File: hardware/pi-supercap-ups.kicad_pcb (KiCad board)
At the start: 2 copper layers, 65 x 56 mm, 69 parts, among them J1 Screw_Terminal_01x04, J2 Raspberry_Pi_2_3, U1 ATtiny13A-SSU, U2 MP1584EN, U3 MT3608, U4 MCP2515-xSO, U5 TJA1051T-3, U6 DS3231M, Y1 8MHz

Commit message: Implement next hardware revision
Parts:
- removed TP3: Vcap, TestPoint:TestPoint_Keystone_5000-5004_Miniature
- added C15: 150pF, Capacitor_SMD:C_0603_1608Metric_Pad1.05x0.95mm_HandSolder, F.Cu at (65.9, 69.1)
- added C16: 47uF, Capacitor_SMD:C_0805_2012Metric_Pad1.15x1.40mm_HandSolder, F.Cu at (65.8, 63.3)
- added C17: 47uF, Capacitor_SMD:C_0805_2012Metric_Pad1.15x1.40mm_HandSolder, F.Cu at (59.2, 55.4)
- added J3: Conn_01x08_Male, Connector_PinHeader_2.54mm:PinHeader_1x08_P2.54mm_Vertical, F.Cu at (66.0, 27.9)
- added J4: Conn_01x02_Male, Connector_PinHeader_2.54mm:PinHeader_1x02_P2.54mm_Vertical, F.Cu at (69.3, 50.0)
- added JP2: SolderJumper_2_Open, custom:SolderJumper-2_P1.3mm_OpenMask_RoundedPad1.0x1.5mm, F.Cu at (69.5, 27.9)
- added JP3: SolderJumper_2_Open, custom:SolderJumper-2_P1.3mm_OpenMask_RoundedPad1.0x1.5mm, F.Cu at (69.5, 43.2)
- added JP4: SolderJumper_2_Open, custom:SolderJumper-2_P1.3mm_OpenMask_RoundedPad1.0x1.5mm, F.Cu at (69.5, 40.6)
- added JP5: SolderJumper_2_Open, custom:SolderJumper-2_P1.3mm_OpenMask_RoundedPad1.0x1.5mm, F.Cu at (69.5, 38.1)
- added JP6: SolderJumper_2_Open, custom:SolderJumper-2_P1.3mm_OpenMask_RoundedPad1.0x1.5mm, F.Cu at (69.5, 33.0)
- added JP7: SolderJumper_3_Open, custom:SolderJumper-3_P1.3mm_OpenMask_RoundedPad1.0x1.5mm, F.Cu at (70.1, 30.5)
- added R17: 15k, Resistor_SMD:R_0603_1608Metric_Pad1.05x0.95mm_HandSolder, F.Cu at (55.5, 67.1)
- added R18: 6.8k, Resistor_SMD:R_0603_1608Metric_Pad1.05x0.95mm_HandSolder, F.Cu at (54.6, 71.3)
- added R19: 10k, Resistor_SMD:R_0603_1608Metric_Pad1.05x0.95mm_HandSolder, F.Cu at (61.5, 71.2)
- added R20: 2.2k, Resistor_SMD:R_0603_1608Metric_Pad1.05x0.95mm_HandSolder, F.Cu at (65.8, 54.2)
- added R21: 2.2k, Resistor_SMD:R_0603_1608Metric_Pad1.05x0.95mm_HandSolder, F.Cu at (65.8, 52.6)
- added TP8: Vbuck, TestPoint:TestPoint_Keystone_5000-5004_Miniature, F.Cu at (62.2, 67.3)
- added TP9: Vboost, TestPoint:TestPoint_Keystone_5000-5004_Miniature, F.Cu at (54.9, 54.2)
- added U7: MT9700, Package_TO_SOT_SMD:SOT-23-5_HandSoldering, F.Cu at (58.0, 71.1)
- C1: value 100nF -> 47uF; footprint Capacitor_SMD:C_0603_1608Metric_Pad1.05x0.95mm_HandSolder -> Capacitor_SMD:C_0805_2012Metric_Pad1.15x1.40mm_HandSolder
- C10: value 22pF -> 100nF
- C12: value 47uF -> 100nF; footprint Capacitor_SMD:C_0805_2012Metric_Pad1.15x1.40mm_HandSolder -> Capacitor_SMD:C_0603_1608Metric_Pad1.05x0.95mm_HandSolder
- C13: value 100nF -> 10uF; footprint Capacitor_SMD:C_0603_1608Metric_Pad1.05x0.95mm_HandSolder -> Capacitor_SMD:C_0805_2012Metric_Pad1.15x1.40mm_HandSolder
- C2: value 10F -> 100nF; footprint Capacitor_THT:CP_Radial_D10.0mm_P5.00mm -> Capacitor_SMD:C_0603_1608Metric_Pad1.05x0.95mm_HandSolder
- C4: value 10uF -> 10F; footprint Capacitor_SMD:C_0805_2012Metric_Pad1.15x1.40mm_HandSolder -> Capacitor_THT:CP_Radial_D10.0mm_P5.00mm
- C5: value 100nF -> 10F; footprint Capacitor_SMD:C_0603_1608Metric_Pad1.05x0.95mm_HandSolder -> Capacitor_THT:CP_Radial_D10.0mm_P5.00mm
- C6: value 150pF -> 10F; footprint Capacitor_SMD:C_0603_1608Metric_Pad1.05x0.95mm_HandSolder -> Capacitor_THT:CP_Radial_D10.0mm_P5.00mm
- C7, C8: value 47uF -> 22pF; footprint Capacitor_SMD:C_0805_2012Metric_Pad1.15x1.40mm_HandSolder -> Capacitor_SMD:C_0603_1608Metric_Pad1.05x0.95mm_HandSolder
- C9: value 22pF -> 47uF; footprint Capacitor_SMD:C_0603_1608Metric_Pad1.05x0.95mm_HandSolder -> Capacitor_SMD:C_0805_2012Metric_Pad1.15x1.40mm_HandSolder
- D1: value RLED -> SMF16CA; footprint LED_SMD:LED_0603_1608Metric_Pad1.05x0.95mm_HandSolder -> Diode_SMD:D_SOD-123F
- D10, D11: value DS34W -> GLED; footprint Diode_SMD:D_SOD-123F -> LED_SMD:LED_0603_1608Metric_Pad1.05x0.95mm_HandSolder
- D12: value RLED -> DS34W; footprint Diode_SMD:D_0603_1608Metric_Pad1.05x0.95mm_HandSolder -> Diode_SMD:D_SOD-123F
- D13, D14: value GLED -> DS34W; footprint LED_SMD:LED_0603_1608Metric_Pad1.05x0.95mm_HandSolder -> Diode_SMD:D_SOD-123F
- D2: value Zener 3V3 -> DS34W; footprint Diode_SMD:D_SOD-123 -> Diode_SMD:D_SOD-123F
- D3: value DS34W -> RLED; footprint Diode_SMD:D_SOD-123F -> Diode_SMD:D_0603_1608Metric_Pad1.05x0.95mm_HandSolder
- D4, D5: value ZMM55C2V7 -> RLED; footprint Diode_SMD:D_MiniMELF_Handsoldering -> Diode_SMD:D_0603_1608Metric_Pad1.05x0.95mm_HandSolder
- D6: value DS34W -> RLED; footprint Diode_SMD:D_SOD-123F -> LED_SMD:LED_0603_1608Metric_Pad1.05x0.95mm_HandSolder
- D7: value RLED -> Zener 3V3; footprint Diode_SMD:D_0603_1608Metric_Pad1.05x0.95mm_HandSolder -> Diode_SMD:D_SOD-123
- D8: value RLED -> ZMM55C2V7; footprint Diode_SMD:D_0603_1608Metric_Pad1.05x0.95mm_HandSolder -> Diode_SMD:D_MiniMELF_Handsoldering
- D9: value DS34W -> ZMM55C2V7; footprint Diode_SMD:D_SOD-123F -> Diode_SMD:D_MiniMELF_Handsoldering
- J1: footprint TerminalBlock_MetzConnect:TerminalBlock_MetzConnect_Type055_RT01504HDWU_1x04_P5.00mm_Horizontal -> custom:15EDGVC-3.81-4P
- L2: value 4.7uH -> 5.6uH
- R1: value 680R -> 4.7k
- R10: value 110k -> 2.2k
- R11: value 15k -> 120R; footprint Resistor_SMD:R_0603_1608Metric_Pad1.05x0.95mm_HandSolder -> Resistor_SMD:R_1206_3216Metric_Pad1.42x1.75mm_HandSolder
- R12: value 1k -> 100k
- R13: value 10k -> 100k
- R14: value 1k -> 40.2k
- R15: value 1k -> 210k
- R16: value 120R -> 110k; footprint Resistor_SMD:R_1206_3216Metric_Pad1.42x1.75mm_HandSolder -> Resistor_SMD:R_0603_1608Metric_Pad1.05x0.95mm_HandSolder
- R2: value 4.7k -> 2.2k
- R3: value 20R -> 2.2k; footprint Resistor_SMD:R_2512_6332Metric_Pad1.52x3.35mm_HandSolder -> Resistor_SMD:R_0603_1608Metric_Pad1.05x0.95mm_HandSolder
- R4: value 1k -> 1.5k
- R5: value 3k -> 4.7k
- R6: value 100k -> 4.7k
- R7: value 100k -> 10k
- R8: value 40.2k -> 10k
- R9: value 210k -> 2.2k
- TP1: value GND -> +12V_prot
- TP2: value Sense_Vcc -> GND
- TP4: value Vout -> Vcap
- U2: value MP1584EN -> MCP2515-xSO; footprint Package_SO:SOIC-8-1EP_3.9x4.9mm_P1.27mm_EP2.35x2.35mm -> Package_SO:SOIC-18W_7.5x11.6mm_P1.27mm
- U3: value MT3608 -> TJA1051T-3; footprint Package_TO_SOT_SMD:SOT-23-6_Handsoldering -> Package_SO:SOIC-8_3.9x4.9mm_P1.27mm
- U4: value MCP2515-xSO -> DS3231M; footprint Package_SO:SOIC-18W_7.5x11.6mm_P1.27mm -> Package_SO:SOIC-16W_7.5x10.3mm_P1.27mm
- U5: value TJA1051T-3 -> MP1584EN; footprint Package_SO:SOIC-8_3.9x4.9mm_P1.27mm -> Package_SO:SOIC-8-1EP_3.9x4.9mm_P1.27mm_EP2.35x2.35mm
- U6: value DS3231M -> MT3608; footprint Package_SO:SOIC-16W_7.5x10.3mm_P1.27mm -> Package_TO_SOT_SMD:SOT-23-6_Handsoldering
- moved C13 64.2 mm to (77.5, 67.3), turned to 0 degrees
- moved R2 56.0 mm to (23.4, 59.3)
- moved D1 52.7 mm to (80.3, 46.8), turned to 90 degrees
- moved R9 51.5 mm to (27.9, 43.8), turned to 90 degrees
- moved D10 49.6 mm to (26.2, 43.8), turned to 90 degrees
- moved R12 49.5 mm to (76.5, 70.5), turned to 270 degrees
- moved C1 48.8 mm to (24.9, 26.9)
- moved D7 47.9 mm to (75.3, 47.1), turned to 270 degrees
- moved D6 47.7 mm to (21.3, 29.9), turned to 90 degrees
- moved R8 46.0 mm to (52.1, 29.0), turned to 270 degrees
- moved D12 45.9 mm to (69.2, 64.3), turned to 180 degrees
- moved TP2 45.6 mm to (32.1, 44.7)
- moved R14 42.8 mm to (69.8, 72.1), turned to 0 degrees
- moved R7 42.7 mm to (54.9, 27.8), turned to 270 degrees
- moved U2 42.4 mm to (45.2, 33.7)
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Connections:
- C1 pad 1: 3.3V -> /5V
- C10 pad 1: /CANbus interface/OSC1 -> GND
- C10 pad 2: GND -> 3.3V
- C11 pad 1: 3.3V -> GND
- C11 pad 2: GND -> /5V
- C12 pad 1: GND -> 3.3V
- C12 pad 2: /5V -> GND
- C13 pad 1: 3.3V -> /inv_Sense_Vcc/+12V
- C14 pad 1: GND -> /Buck converter/SW
- C14 pad 2: 3.3V -> /Buck converter/BST
- C2 pad 1: /Power Bank/Vcap -> 3.3V
- C2 pad 2: /Power Bank/Vc1 -> GND
- C3 pad 1: /Power Bank/Vc1 -> /Power Bank/Vcap
- C3 pad 2: GND -> /Power Bank/Vc1
- C4 pad 1: /Voltage input/+12V_protected -> /Power Bank/Vc1
- C5 pad 1: /Voltage input/SW -> /Power Bank/Vcap
- C5 pad 2: /Voltage input/BST -> /Power Bank/Vc1
- C6 pad 1: /Voltage input/COMP -> /Power Bank/Vc1
- C6 pad 2: Net-(C6-Pad2) -> GND
- C7 pad 1: /Power Bank/Vin -> GND
- C7 pad 2: GND -> /CANbus interface/OSC2
- C8 pad 1: /5V -> /CANbus interface/OSC1
- C9 pad 1: GND -> 3.3V
- C9 pad 2: /CANbus interface/OSC2 -> GND
- D1 pad 1: GND -> /12V_fused
- D1 pad 2: Net-(D1-Pad2) -> GND
- D10 pad 1: /Voltage input/SW -> GND
- D10 pad 2: GND -> Net-(D10-Pad2)
- D11 pad 1: /5V -> GND
- D11 pad 2: /Voltage output/SW -> Net-(D11-Pad2)
- D12 pad 1: GND -> /Buck converter/SW
- D12 pad 2: Net-(D12-Pad2) -> GND
- D13 pad 1: GND -> /5V
- D13 pad 2: Net-(D13-Pad2) -> /Current limiting/Vin
- D14 pad 1: GND -> /5V
- D14 pad 2: Net-(D14-Pad2) -> /Boost converter/SW
- D2 pad 1: /Sense_Vcc -> /inv_Sense_Vcc/+12V
- D2 pad 2: GND -> /12V_fused
- D3 pad 1: /Power Bank/Vout -> GND
- D3 pad 2: /Power Bank/Vin -> Net-(D3-Pad2)
- D4 pad 1: /Power Bank/Vcap -> GND
- D4 pad 2: /Power Bank/Vc1 -> Net-(D4-Pad2)
- D5 pad 1: /Power Bank/Vc1 -> GND
- D5 pad 2: GND -> Net-(D5-Pad2)
- D6 pad 1: /Power Bank/Vout -> GND
- D6 pad 2: /Power Bank/Vcap -> Net-(D6-Pad2)
- D7 pad 1: GND -> /Sense_Vcc
- D7 pad 2: Net-(D7-Pad2) -> GND
- D8 pad 1: GND -> /Power Bank/Vcap
- D8 pad 2: Net-(D8-Pad2) -> /Power Bank/Vc1
- D9 pad 1: /Voltage input/+12V_protected -> /Power Bank/Vc1
- D9 pad 2: /Voltage input/12V_fused -> GND
- F1 pad 1: /Voltage input/12V_fused -> /12V_fused
- J2 pad 35: /MISO -> /GPIO19
- J2 pad 36: /ATTiny_RESET -> /GPIO16
- J2 pad 37: /Sense_Vcc -> /GPIO26
- J2 pad 38: /inv_Sense_EN -> /GPIO20
- J2 pad 40: /ATSCK -> /GPIO21
- L1 pad 1: /Voltage input/SW -> /Buck converter/SW
- L1 pad 2: /Power Bank/Vin -> /Current limiting/Vin
- L2 pad 1: /Power Bank/Vout -> /Power Bank/Vcap
- L2 pad 2: /Voltage output/SW -> /Boost converter/SW
- R1 pad 1: 3.3V -> /inv_Sense_Vcc/+12V
- R1 pad 2: Net-(D1-Pad2) -> Net-(D3-Pad2)
- R10 pad 1: /5V -> /CANbus interface/RX
- R10 pad 2: /Voltage output/FB -> Net-(D11-Pad2)
- R11 pad 1: /Voltage output/FB -> Net-(JP1-Pad2)
- R11 pad 2: GND -> /CAN_H
- R12 pad 1: /5V -> /Buck converter/FREQ
- R12 pad 2: Net-(D12-Pad2) -> GND
- R13 pad 1: 3.3V -> Net-(C15-Pad2)
- R13 pad 2: Net-(R13-Pad2) -> GND
- R14 pad 1: /CANbus interface/TX -> /Buck converter/FB
- R14 pad 2: Net-(D13-Pad2) -> GND
- R15 pad 1: /CANbus interface/RX -> /Buck converter/FB
- R15 pad 2: Net-(D14-Pad2) -> /5V
- R16 pad 1: Net-(JP1-Pad2) -> /Boost converter/SW
- R16 pad 2: /CAN_H -> /Boost converter/FB
- R2 pad 1: /Voltage input/+12V_protected -> /Power Bank/Vcap
- R2 pad 2: /Sense_Vcc -> Net-(D4-Pad2)
- R3 pad 1: /Power Bank/Vout -> /5V
- R3 pad 2: /Power Bank/Vcap -> Net-(D5-Pad2)
- R4 pad 1: /Power Bank/Vcap -> 3.3V
- R4 pad 2: Net-(D7-Pad2) -> Net-(D6-Pad2)
- R5 pad 1: /Voltage input/+12V_protected -> /Sense_Vcc
- R5 pad 2: Net-(D8-Pad2) -> GND
- R6 pad 1: /Voltage input/FREQ -> /inv_Sense_Vcc/+12V
- R6 pad 2: GND -> /Sense_Vcc
- R7 pad 1: Net-(C6-Pad2) -> 3.3V
- R7 pad 2: GND -> /ATTiny_RESET
- R8 pad 1: /Voltage input/FB -> 3.3V
- R8 pad 2: GND -> Net-(R8-Pad2)
- R9 pad 1: /Voltage input/FB -> /CANbus interface/TX
- R9 pad 2: /Power Bank/Vin -> Net-(D10-Pad2)
- TP1 pad 1: GND -> /inv_Sense_Vcc/+12V
- TP2 pad 1: /Sense_Vcc -> GND
- TP4 pad 1: /Power Bank/Vout -> /Power Bank/Vcap
- U1 pad 2: /Sense_Vcc -> /PB3
- U1 pad 3: /GPIO3 -> /PB4
- U1 pad 5: /inv_Sense_EN -> /MOSI
- U2 pad 1: /Voltage input/SW -> /CANbus interface/TX
- U2 pad 2: (no net) -> /CANbus interface/RX
- U2 pad 3: /Voltage input/COMP -> (no net)
- U2 pad 4: /Voltage input/FB -> (no net)
- U2 pad 5: GND -> (no net)
- U2 pad 6: /Voltage input/FREQ -> (no net)
- U2 pad 7: /Voltage input/+12V_protected -> /CANbus interface/OSC2
- U2 pad 8: /Voltage input/BST -> /CANbus interface/OSC1
- U2 pad 9: (no net) -> GND
- U3 pad 1: /Voltage output/SW -> /CANbus interface/TX
- U3 pad 3: /Voltage output/FB -> /5V
- U3 pad 4: /Power Bank/Vout -> /CANbus interface/RX
- U3 pad 5: /Power Bank/Vout -> 3.3V
- U3 pad 6: (no net) -> /CAN_L
- U4 pad 1: /CANbus interface/TX -> (no net)
- U4 pad 10: (no net) -> GND
- U4 pad 11: (no net) -> GND
- U4 pad 12: /INT -> GND
- U4 pad 13: /SCK -> GND
- U4 pad 14: /SI -> /RTC interface/VBAT
- U4 pad 15: /SO -> /SDA1
- U4 pad 16: /CS -> /GPIO3
- U4 pad 2: /CANbus interface/RX -> 3.3V
- U4 pad 5: (no net) -> GND
- U4 pad 6: (no net) -> GND
- U4 pad 7: /CANbus interface/OSC2 -> GND
- U4 pad 8: /CANbus interface/OSC1 -> GND
- U5 pad 1: /CANbus interface/TX -> /Buck converter/SW
- U5 pad 2: GND -> (no net)
- U5 pad 3: /5V -> /Buck converter/COMP
- U5 pad 4: /CANbus interface/RX -> /Buck converter/FB
- U5 pad 5: 3.3V -> GND
- U5 pad 6: /CAN_L -> /Buck converter/FREQ
- U5 pad 7: /CAN_H -> /inv_Sense_Vcc/+12V
- U5 pad 8: GND -> /Buck converter/BST
- U6 pad 1: (no net) -> /Boost converter/SW
- U6 pad 2: 3.3V -> GND
- U6 pad 3: (no net) -> /Boost converter/FB
- U6 pad 4: (no net) -> /Power Bank/Vcap
- U6 pad 5: GND -> /Power Bank/Vcap
- U6 pad 6: GND -> (no net)
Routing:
- net /inv_Sense_Vcc/+12V: track 0.00 -> 99.4 mm, vias 0 -> 6
- net /Voltage input/+12V_protected: track 80.5 -> 0.00 mm, vias 4 -> 0
- net /5V: track 116.2 -> 148.4 mm, vias 8 -> 9
- net /Power Bank/Vin: track 29.3 -> 0.00 mm, vias 2 -> 0
- net /GPIO21: track 0.00 -> 28.2 mm, vias 0 -> 1
- net 3.3V: track 113.4 -> 86.8 mm
- net /Power Bank/Vout: track 26.5 -> 0.00 mm
- net /Power Bank/Vc1: track 19.7 -> 41.7 mm, vias 0 -> 2
- net /CANbus interface/TX: track 73.1 -> 51.3 mm, vias 6 -> 4
- net /PB3: track 0.00 -> 21.1 mm, vias 0 -> 4
- net /GPIO20: track 0.00 -> 20.6 mm, vias 0 -> 1
- net /Power Bank/Vcap: track 52.4 -> 72.1 mm
- net /GPIO19: track 0.00 -> 19.6 mm, vias 0 -> 1
- net /Sense_Vcc: track 52.2 -> 33.8 mm, vias 4 -> 3
- net /Current limiting/Vin: track 0.00 -> 17.9 mm
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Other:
- outline, holes or cut-outs redrawn
- board text added: "+"
- board text added: "-"
- board text added: "H"
- board text added: "L"
- board text added: "Pi Super UPS revD Matti Airas 2019"
- board text removed: "12V"
- board text removed: "3.3V"
- board text removed: "5V"
- board text removed: "Pi Super UPS revC Matti Airas 2019"
- board text removed: "RX"
- board text removed: "TX"
- board text removed: "Vcap"

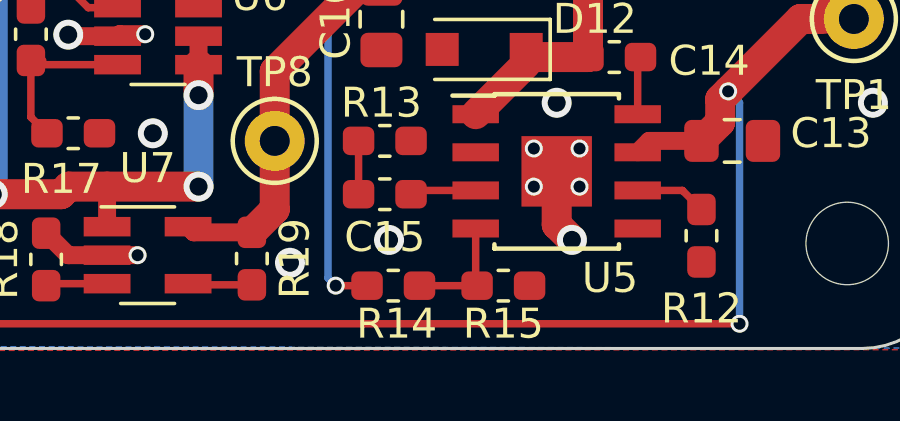
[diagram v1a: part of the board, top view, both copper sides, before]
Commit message: fix a silk screen error by swapping R14 and R15
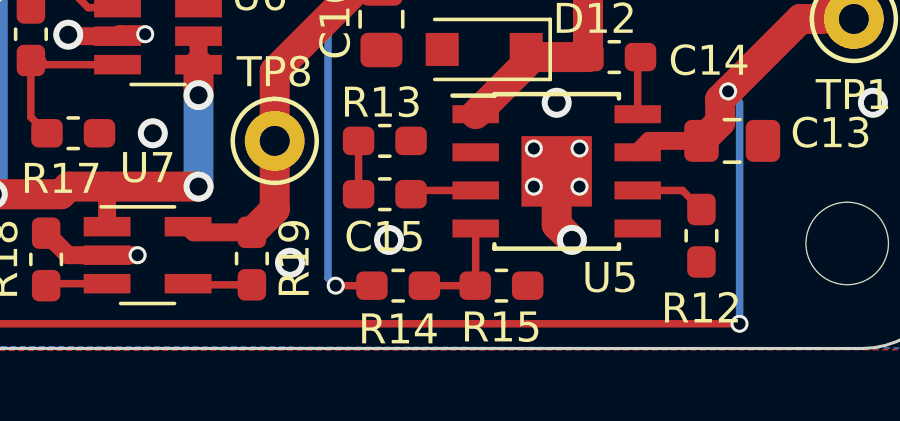
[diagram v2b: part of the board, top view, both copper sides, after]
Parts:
- R14: value 40.2k -> 210k
- R15: value 210k -> 40.2k
- moved R15 3.61 mm to (69.8, 72.1), turned to 0 degrees
- moved R14 3.51 mm to (66.3, 72.1), turned to 180 degrees
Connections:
- J2 pad 10: (no net) -> Net-(J2-Pad10)
- J2 pad 11: (no net) -> Net-(J2-Pad11)
- J2 pad 12: (no net) -> Net-(J2-Pad12)
- J2 pad 13: (no net) -> Net-(J2-Pad13)
- J2 pad 15: (no net) -> Net-(J2-Pad15)
- J2 pad 16: (no net) -> Net-(J2-Pad16)
- J2 pad 18: (no net) -> Net-(J2-Pad18)
- J2 pad 26: (no net) -> Net-(J2-Pad26)
- J2 pad 27: (no net) -> Net-(J2-Pad27)
- J2 pad 28: (no net) -> Net-(J2-Pad28)
- J2 pad 29: (no net) -> Net-(J2-Pad29)
- J2 pad 31: (no net) -> Net-(J2-Pad31)
- J2 pad 32: (no net) -> Net-(J2-Pad32)
- J2 pad 33: (no net) -> Net-(J2-Pad33)
- J2 pad 7: (no net) -> Net-(J2-Pad7)
- J2 pad 8: (no net) -> Net-(J2-Pad8)
- R14 pad 2: GND -> /5V
- R15 pad 2: /5V -> GND
- U2 pad 10: (no net) -> Net-(U2-Pad10)
- U2 pad 11: (no net) -> Net-(U2-Pad11)
- U2 pad 3: (no net) -> Net-(U2-Pad3)
- U2 pad 4: (no net) -> Net-(U2-Pad4)
- U2 pad 5: (no net) -> Net-(U2-Pad5)
- U2 pad 6: (no net) -> Net-(U2-Pad6)
- U4 pad 1: (no net) -> Net-(U4-Pad1)
- U4 pad 3: (no net) -> Net-(U4-Pad3)
- U4 pad 4: (no net) -> Net-(U4-Pad4)
- U5 pad 2: (no net) -> Net-(U5-Pad2)

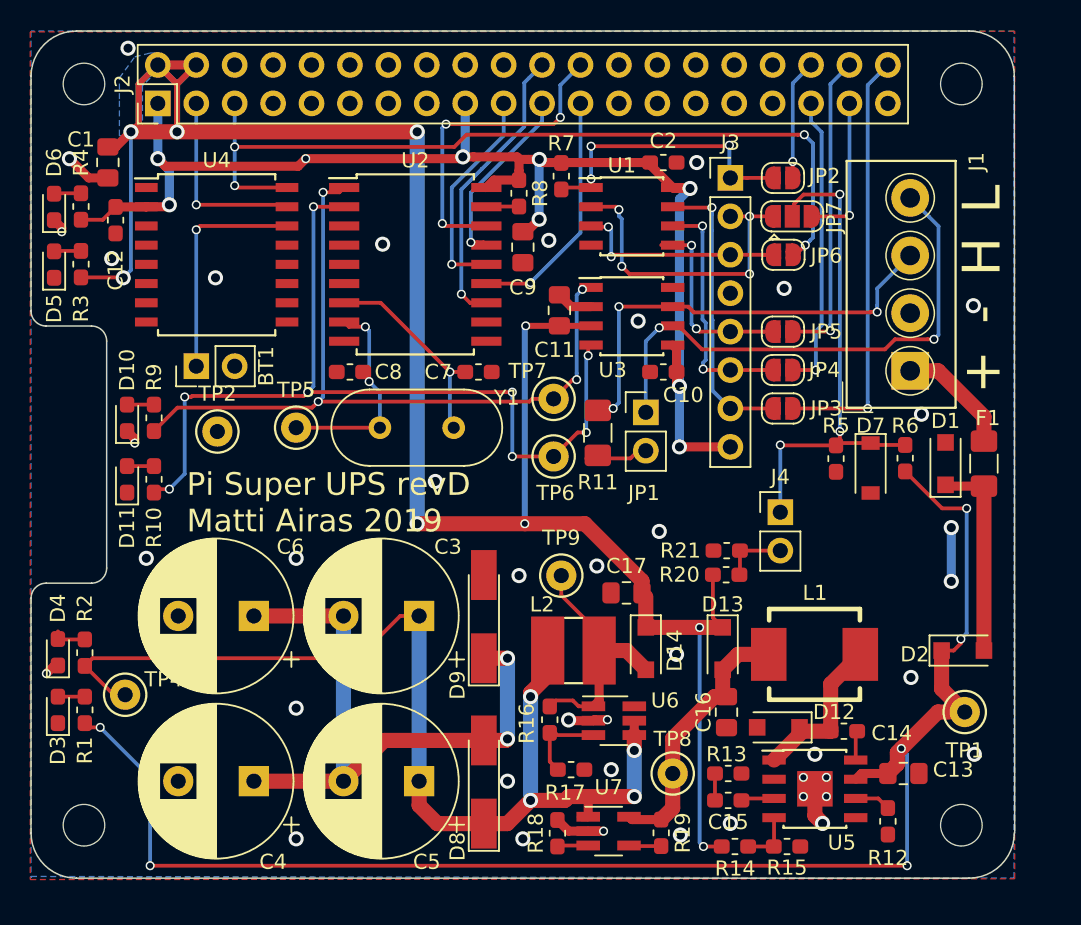
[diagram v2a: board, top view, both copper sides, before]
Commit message: Changed to pure-serial topology. Changed to beefier mcu.
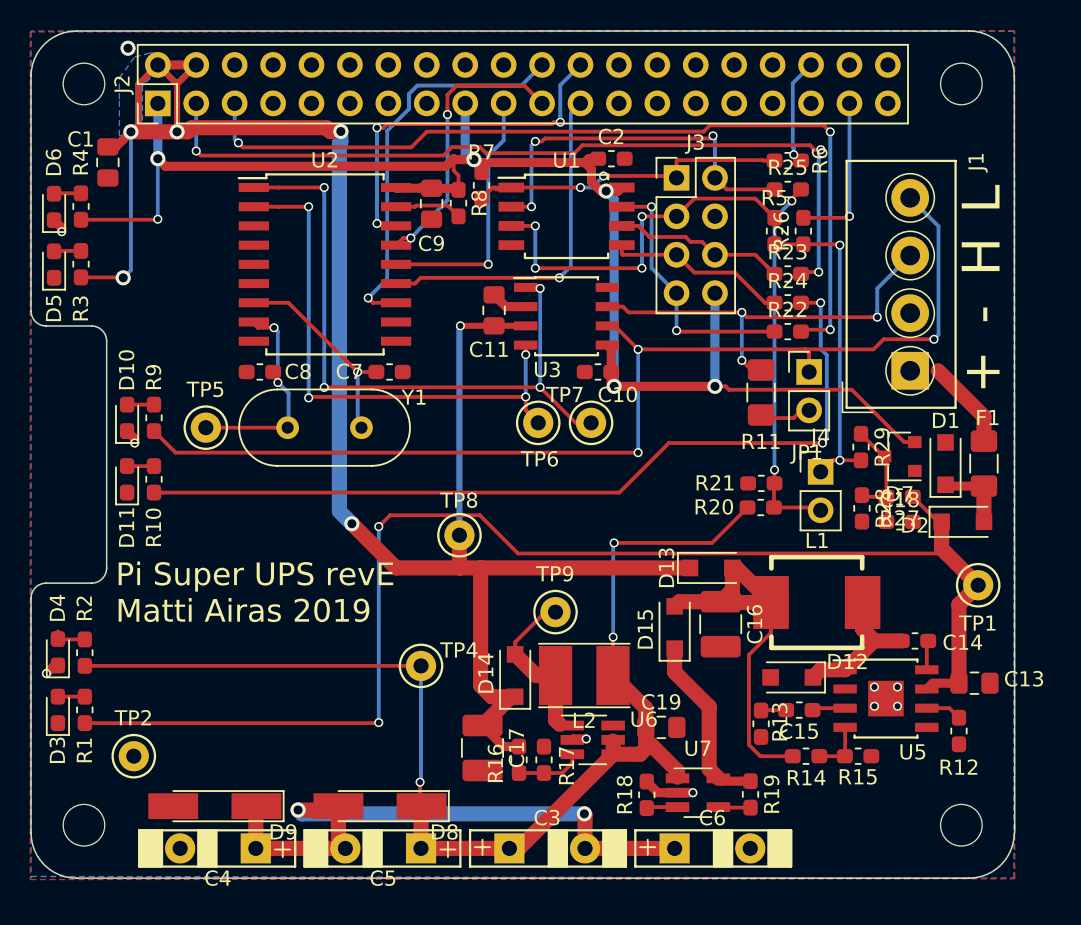
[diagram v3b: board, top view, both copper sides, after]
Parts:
- removed BT1: CR1220 3V, Connector_PinHeader_2.54mm:PinHeader_1x02_P2.54mm_Vertical
- removed C12: 100nF, Capacitor_SMD:C_0603_1608Metric_Pad1.05x0.95mm_HandSolder
- removed JP2, JP3, JP4, JP5, JP6: SolderJumper_2_Open, custom:SolderJumper-2_P1.3mm_OpenMask_RoundedPad1.0x1.5mm
- removed JP7: SolderJumper_3_Open, custom:SolderJumper-3_P1.3mm_OpenMask_RoundedPad1.0x1.5mm
- removed U4: DS3231M, Package_SO:SOIC-16W_7.5x10.3mm_P1.27mm
- added C18: 100nF, Capacitor_SMD:C_0603_1608Metric_Pad1.05x0.95mm_HandSolder, F.Cu at (77.2, 50.7)
- added C19: 22uF, Capacitor_SMD:C_0805_2012Metric_Pad1.15x1.40mm_HandSolder, F.Cu at (61.5, 64.3)
- added D15: DS34W, Diode_SMD:D_SOD-123F, F.Cu at (62.4, 57.7)
- added R22: 0, Resistor_SMD:R_0603_1608Metric_Pad1.05x0.95mm_HandSolder, F.Cu at (69.8, 38.1)
- added R23: 0, Resistor_SMD:R_0603_1608Metric_Pad1.05x0.95mm_HandSolder, F.Cu at (69.8, 34.3)
- added R24: 0, Resistor_SMD:R_0603_1608Metric_Pad1.05x0.95mm_HandSolder, F.Cu at (69.8, 36.2)
- added R25: 0, Resistor_SMD:R_0603_1608Metric_Pad1.05x0.95mm_HandSolder, F.Cu at (69.8, 28.7)
- added R26: 0, Resistor_SMD:R_0603_1608Metric_Pad1.05x0.95mm_HandSolder, F.Cu at (70.9, 31.5)
- added R27: 4.7k, Resistor_SMD:R_0603_1608Metric_Pad1.05x0.95mm_HandSolder, F.Cu at (77.2, 49.0)
- added R28: 10k, Resistor_SMD:R_0603_1608Metric_Pad1.05x0.95mm_HandSolder, F.Cu at (74.7, 49.8)
- added R29: 10k, Resistor_SMD:R_0603_1608Metric_Pad1.05x0.95mm_HandSolder, F.Cu at (74.7, 45.7)
- C16, C17: value 47uF -> 100uF; footprint Capacitor_SMD:C_0805_2012Metric_Pad1.15x1.40mm_HandSolder -> Capacitor_SMD:C_1210_3225Metric_Pad1.42x2.65mm_HandSolder
- C3, C4, C5, C6: footprint Capacitor_THT:CP_Radial_D10.0mm_P5.00mm -> custom:CP_Radial_D10.0mm_P5.00mm_flat
- D11: value GLED -> RLED
- D7: value Zener 3V3 -> BAT54S; footprint Diode_SMD:D_SOD-123 -> Package_TO_SOT_SMD:SOT-23
- J3: footprint Connector_PinHeader_2.54mm:PinHeader_1x08_P2.54mm_Vertical -> Connector_PinHeader_2.54mm:PinHeader_2x04_P2.54mm_Vertical
- L2: footprint Inductor_SMD:L_4.5x4.8_H3_Handsolder -> Inductor_SMD:L_Taiyo-Yuden_NR-40xx_HandSoldering
- R10: value 2.2k -> 1.5k
- R14: value 210k -> 232k
- R5, R6: value 4.7k -> 0
- U1: value ATtiny13A-SSU -> ATtiny25-20SU; footprint Package_SO:SOIC-8_3.9x4.9mm_P1.27mm -> Package_SO:SOIJ-8_5.3x5.3mm_P1.27mm
- moved C6 31.8 mm to (62.4, 72.3), turned to 0 degrees
- moved TP2 22.2 mm to (26.6, 66.2)
- moved D9 21.8 mm to (32.0, 69.5), turned to 180 degrees
- moved R6 21.1 mm to (69.8, 26.8), turned to 0 degrees
- moved TP8 21.1 mm to (48.1, 51.6)
- moved TP4 19.7 mm to (45.6, 60.2)
- moved C3 16.5 mm to (51.4, 72.3), turned to 0 degrees
- moved R5 15.6 mm to (69.0, 31.5)
- moved C17 14.0 mm to (49.7, 65.6), turned to 270 degrees
- moved JP1 11.1 mm to (71.2, 40.8)
- moved R11 11.1 mm to (68.1, 42.1)
- moved D14 8.82 mm to (51.8, 60.8), turned to 90 degrees
- moved D2 8.51 mm to (81.4, 50.7)
- moved TP1 8.43 mm to (82.4, 54.9)
- moved R12 7.60 mm to (81.2, 64.5)
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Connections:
- net /2.5V renamed /Vcap:2
- net /ATSCK renamed /PB2
- net /MISO renamed /PB1
- net /MOSI renamed /PB0
- C16 pad 1: /Current limiting/Vin -> /Buck converter/Vout
- C3 pad 1: /Power Bank/Vcap -> /Vcap
- C5 pad 1: /Power Bank/Vcap -> /Vcap
- D13 pad 2: /Current limiting/Vin -> /Buck converter/Vout
- D7 pad 1: /Sense_Vcc -> GND
- D7 pad 2: GND -> 3.3V
- D8 pad 1: /Power Bank/Vcap -> /Vcap
- J2 pad 10: Net-(J2-Pad10) -> (no net)
- J2 pad 11: Net-(J2-Pad11) -> (no net)
- J2 pad 12: Net-(J2-Pad12) -> (no net)
- J2 pad 13: Net-(J2-Pad13) -> (no net)
- J2 pad 15: Net-(J2-Pad15) -> (no net)
- J2 pad 16: Net-(J2-Pad16) -> (no net)
- J2 pad 18: Net-(J2-Pad18) -> (no net)
- J2 pad 26: Net-(J2-Pad26) -> (no net)
- J2 pad 27: Net-(J2-Pad27) -> (no net)
- J2 pad 28: Net-(J2-Pad28) -> (no net)
- J2 pad 29: Net-(J2-Pad29) -> (no net)
- J2 pad 3: /SDA1 -> /GPIO2
- J2 pad 31: Net-(J2-Pad31) -> (no net)
- J2 pad 32: Net-(J2-Pad32) -> (no net)
- J2 pad 33: Net-(J2-Pad33) -> (no net)
- J2 pad 35: /GPIO19 -> (no net)
- J2 pad 38: /GPIO20 -> (no net)
- J2 pad 40: /GPIO21 -> (no net)
- J2 pad 7: Net-(J2-Pad7) -> (no net)
- J2 pad 8: Net-(J2-Pad8) -> (no net)
- L1 pad 2: /Current limiting/Vin -> /Buck converter/Vout
- L2 pad 1: /Power Bank/Vcap -> /Vcap
- R10 pad 1: /CANbus interface/RX -> /ATTiny_LED
- R14 pad 2: /5V -> /Buck converter/Vout
- R16 pad 1: /Boost converter/SW -> /5V
- R2 pad 1: /Power Bank/Vcap -> /Vcap
- R20 pad 1: /5V -> /Vcap
- R5 pad 1: /Sense_Vcc -> /PB4
- R5 pad 2: GND -> /Sense_Vcc
- R6 pad 1: /inv_Sense_Vcc/+12V -> /ATTiny_RESET
- R6 pad 2: /Sense_Vcc -> /GPIO16
- R9 pad 1: /CANbus interface/TX -> /CAN_L
- TP4 pad 1: /Power Bank/Vcap -> /Vcap
- TP8 pad 1: /Current limiting/Vin -> /5V
- U2 pad 10: Net-(U2-Pad10) -> (no net)
- U2 pad 11: Net-(U2-Pad11) -> (no net)
- U2 pad 3: Net-(U2-Pad3) -> (no net)
- U2 pad 4: Net-(U2-Pad4) -> (no net)
- U2 pad 5: Net-(U2-Pad5) -> (no net)
- U2 pad 6: Net-(U2-Pad6) -> (no net)
- U5 pad 2: Net-(U5-Pad2) -> (no net)
- U6 pad 4: /Power Bank/Vcap -> /Vcap
- U6 pad 5: /Power Bank/Vcap -> /Vcap
- U7 pad 1: /Power Bank/Vcap -> /Vcap
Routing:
- net /Vcap: track 0.00 -> 81.8 mm, vias 0 -> 4
- net /Power Bank/Vcap: track 72.1 -> 0.00 mm, vias 4 -> 0
- net /ATTiny_LED: track 0.00 -> 56.4 mm, vias 0 -> 2
- net /GPIO2: track 0.00 -> 54.7 mm, vias 0 -> 3
- net /CAN_L: track 35.3 -> 74.1 mm, vias 2 -> 3
- net /GPIO21: track 28.2 -> 0.00 mm, vias 1 -> 0
- net /Buck converter/Vout: track 0.00 -> 25.8 mm
- net /CANbus interface/RX: track 59.6 -> 36.1 mm, vias 8 -> 4
- net /Vcap:2: track 4.28 -> 24.9 mm, vias 0 -> 2
- net /GPIO20: track 20.6 -> 0.00 mm, vias 1 -> 0
- net /GPIO19: track 19.6 -> 0.00 mm, vias 1 -> 0
- net 3.3V: track 86.8 -> 102.2 mm, vias 9 -> 6
- net /RTC interface/VBAT: track 15.1 -> 0.00 mm, vias 1 -> 0
- net /SDA1: track 12.9 -> 0.00 mm, vias 1 -> 0
- net /Sense_Vcc: track 33.8 -> 21.5 mm, vias 3 -> 2
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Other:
- board text added: "Pi Super UPS revE Matti Airas 2019"
- board text removed: "Pi Super UPS revD Matti Airas 2019"
